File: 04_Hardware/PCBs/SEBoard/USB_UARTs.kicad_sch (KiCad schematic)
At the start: 38 parts, among them J10 67996-100HLF, J5 USB4080-03-A, J6 22-28-4034, J9 22-28-4034, U1 SC200EEMNA-E53-UGNDA

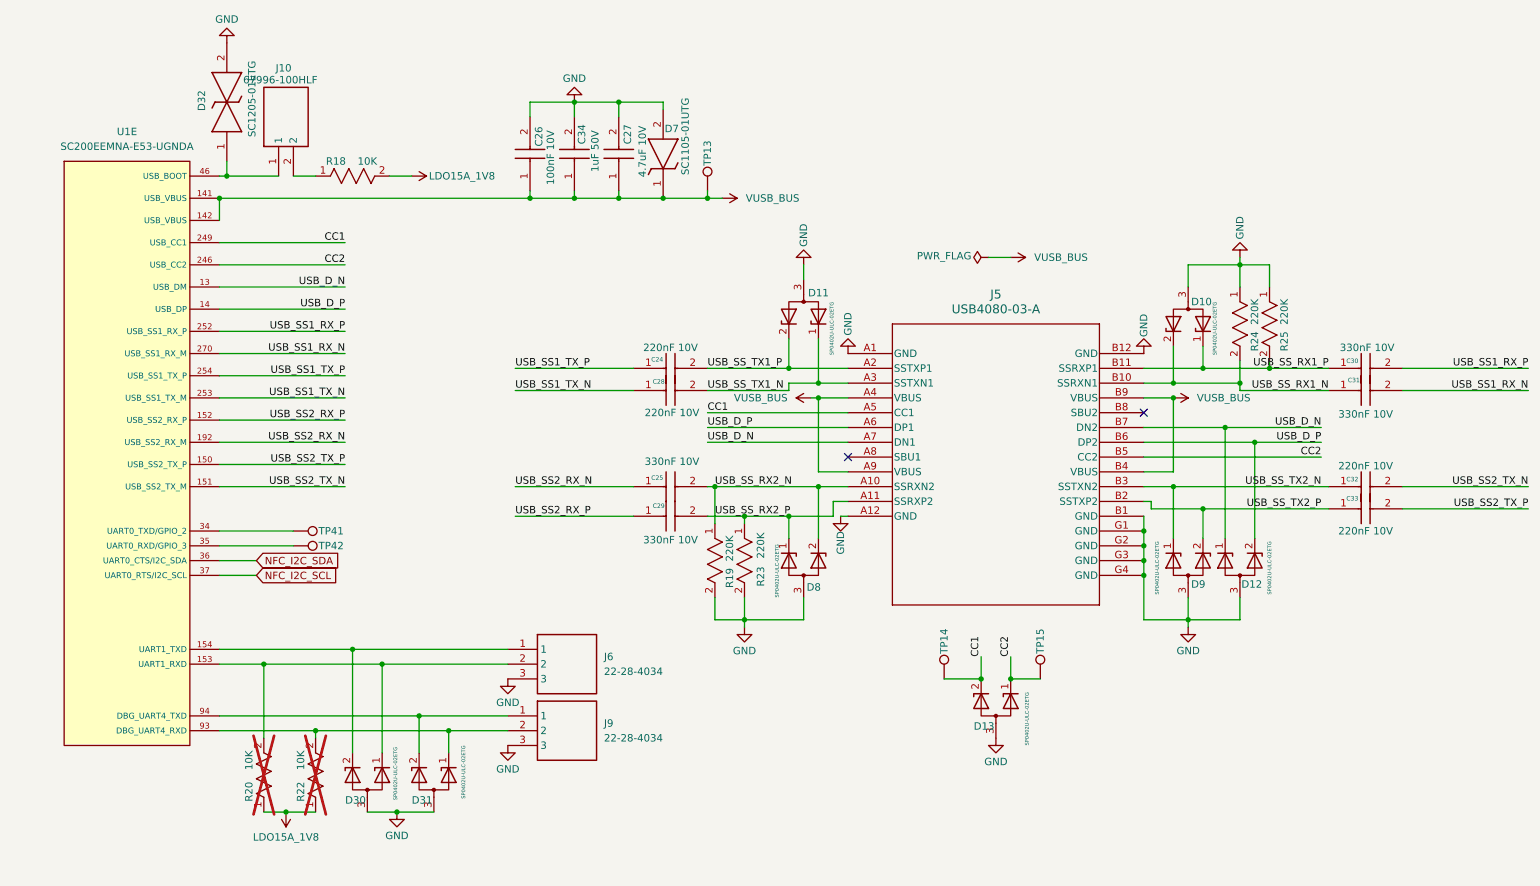
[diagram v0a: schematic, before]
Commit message: feat(schematic): add SE250B4 symbol to schematic (unchecked)
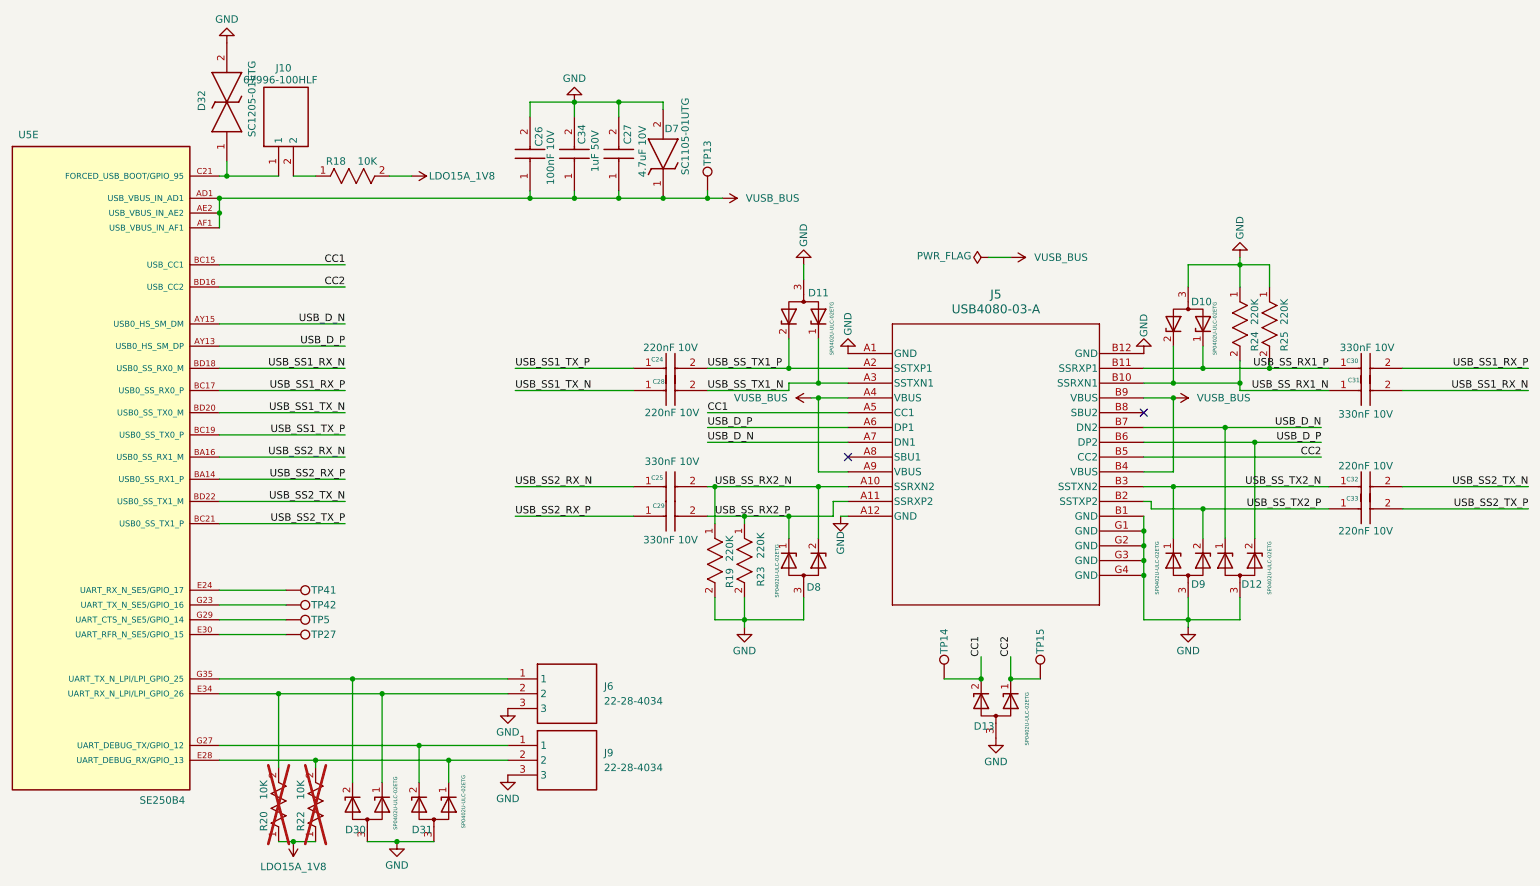
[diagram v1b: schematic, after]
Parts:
- removed U1: SC200EEMNA-E53-UGNDA, SEBoard:SC200E_SC206E, symbol SEBoard:SC200E
- added TP27, TP5: Sens_M, TestPoint:TestPoint_Pad_D1.0mm, symbol SEBoard:TestPoint
- added U5: SE250B4, 000MCLib:XCVR_SE250B4-NA, symbol 000MCLib:SE250B4
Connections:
- net CC1: now also U5.BC15 (USB_CC1)
- net CC2: now also U5.BD16 (USB_CC2)
- net USB_D_N: now also U5.AY15 (USB0_HS_SM_DM)
- net USB_D_P: now also U5.AY13 (USB0_HS_SM_DP)
- net USB_SS1_RX_N: now also U5.BD18 (USB0_SS_RX0_M)
- net USB_SS1_RX_P: now also U5.BC17 (USB0_SS_RX0_P)
- net USB_SS1_TX_N: now also U5.BD20 (USB0_SS_TX0_M)
- net USB_SS1_TX_P: now also U5.BC19 (USB0_SS_TX0_P)
- net USB_SS2_RX_N: now also U5.BA16 (USB0_SS_RX1_M)
- net USB_SS2_RX_P: now also U5.BA14 (USB0_SS_RX1_P)
- net USB_SS2_TX_N: now also U5.BD22 (USB0_SS_TX1_M)
- net USB_SS2_TX_P: now also U5.BC21 (USB0_SS_TX1_P)
- net VUSB_BUS: now also U5.AD1 (USB_VBUS_IN_AD1), U5.AE2 (USB_VBUS_IN_AE2), U5.AF1 (USB_VBUS_IN_AF1)
- net at D30.2 (K_2), J6.1: now also U5.G35 (UART_TX_N_LPI/LPI_GPIO_25)
- net at D30.1 (K_1), J6.2, R20.2: now also U5.E34 (UART_RX_N_LPI/LPI_GPIO_26)
- net at TP41.1: now also U5.E24 (UART_RX_N_SE5/GPIO_17)
- net at TP42.1: now also U5.G23 (UART_TX_N_SE5/GPIO_16)
- net at D32.1, J10.1: now also U5.C21 (FORCED_USB_BOOT/GPIO_95)
- net at D31.1 (K_1), J9.2, R22.2: now also U5.E28 (UART_DEBUG_RX/GPIO_13)
- net at D31.2 (K_2), J9.1: now also U5.G27 (UART_DEBUG_TX/GPIO_12)
- new net: TP27.1, U5.E30 (UART_RFR_N_SE5/GPIO_15)
- new net: TP5.1, U5.G29 (UART_CTS_N_SE5/GPIO_14)
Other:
- moved on the sheet: D30, D31, J6, J9, R20, R22, TP41, TP42

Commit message: feat: Updated schematic layout and moved new components to Layout
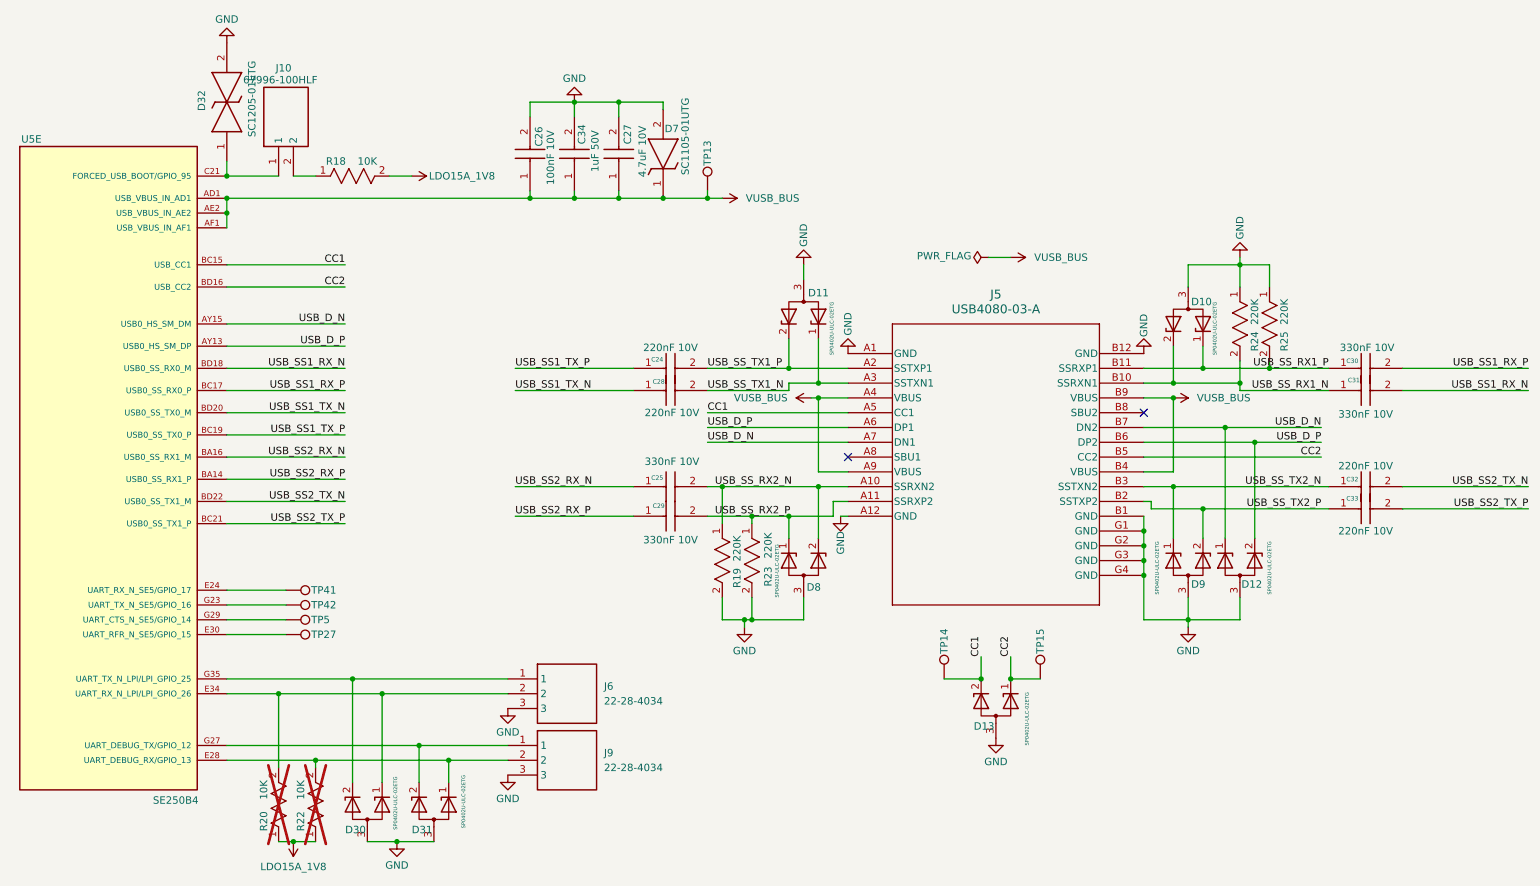
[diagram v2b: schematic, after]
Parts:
- C24, C28, C32, C33: footprint SEBoard:CAPC1005X55N -> 000MCLib:CAPC1005X55N; symbol SEBoard:GRM155R61A224JE19D -> 000MCLib:GRM155R61A224JE19D
- C25, C29, C30, C31: footprint SEBoard:CAPC1005X55N -> 000MCLib:CAPC1005X55N; symbol SEBoard:GRM155R61A334KE15D -> 000MCLib:GRM155R61A334KE15D
- C26: footprint SEBoard:CAPC1005X55N -> 000MCLib:CAPC1005X55N; symbol SEBoard:GRM155R71A104KA01D -> 000MCLib:GRM155R71A104KA01D
- C27: footprint SEBoard:CAPC1608X90N -> 000MCLib:CAPC1608X90N; symbol SEBoard:LMK107BJ475KA-T -> 000MCLib:LMK107BJ475KA-T
- C34: footprint SEBoard:CAPC1005X55N -> 000MCLib:CAPC1005X55N; symbol SEBoard:GRM155R61H105KE05D -> 000MCLib:GRM155R61H105KE05D
- D10, D11, D12, D13, D30, D31, D8, D9: footprint SEBoard:SESD0402Q2UG0020090 -> 000MCLib:SESD0402Q2UG0020090; symbol SEBoard:SP0402U-ULC-02ETG -> 000MCLib:SP0402U-ULC-02ETG
- D32: footprint SEBoard:SC120501ETG -> 000MCLib:SC120501ETG; symbol SEBoard:SC1205-01ETG -> 000MCLib:SC1205-01ETG
- D7: footprint SEBoard:SC110501UTG -> 000MCLib:SC110501UTG; symbol SEBoard:SC1105-01UTG -> 000MCLib:SC1105-01UTG
- J10: footprint SEBoard:HDRV2W67P254_2X1_254X483X858P -> 000MCLib:HDRV2W67P254_2X1_254X483X858P; symbol SEBoard:67996-100HLF -> 000MCLib:67996-100HLF
- J5: footprint SEBoard:GCT_USB4080-03-A_REVA -> 000MCLib:GCT_USB4080-03-A_REVA; symbol SEBoard:USB4080-03-A -> 000MCLib:USB4080-03-A
- J6, J9: footprint SEBoard:HDRV3W66P0X254_1X3_762X249X1042P -> 000MCLib:HDRV3W66P0X254_1X3_762X249X1042P; symbol SEBoard:22-28-4034 -> 000MCLib:22-28-4034
- R18, R20, R22: footprint SEBoard:RC0402N_YAG -> 000MCLib:RC0402N_YAG; symbol SEBoard:RC0402JR-0710KL -> 000MCLib:RC0402JR-0710KL
- R19, R23, R24, R25: footprint SEBoard:RC0402N_YAG -> 000MCLib:RC0402N_YAG; symbol SEBoard:RC0402FR-07220KL -> 000MCLib:RC0402FR-07220KL
- TP13, TP14, TP15, TP27, TP41, TP42, TP5: symbol SEBoard:TestPoint -> 000MCLib:TestPoint
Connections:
- net USB_SS_RX2_N: no longer C29.2, D8.1 (K_1), J5.A11 (SSRXP2), R23.1
- new net USB_SS_RX2_P: C29.2, D8.1 (K_1), J5.A11 (SSRXP2), R23.1
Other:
- moved on the sheet: R19, R23, U5E
